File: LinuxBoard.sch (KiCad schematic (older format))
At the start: 0 parts

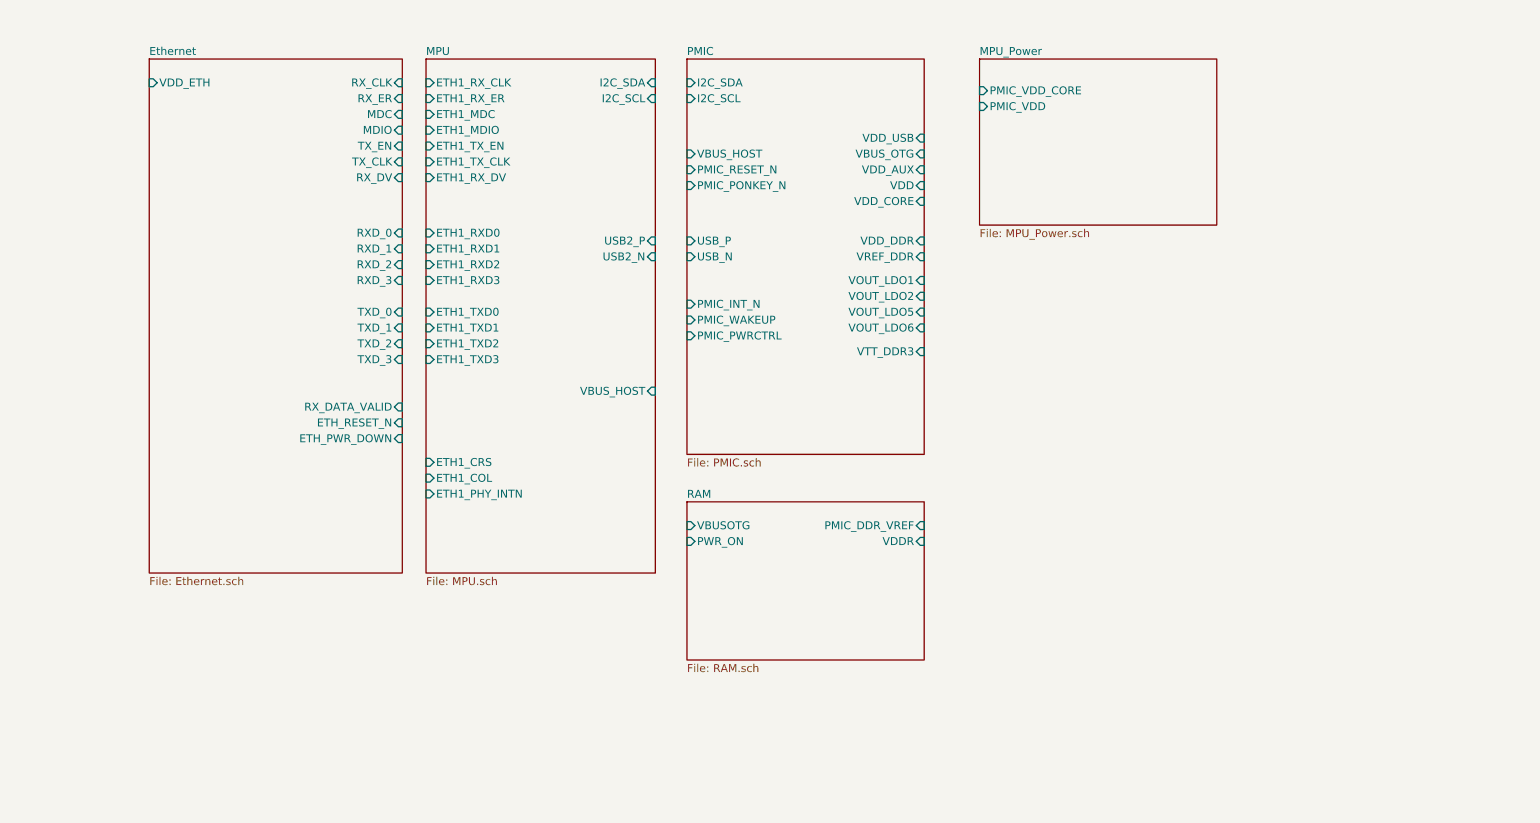
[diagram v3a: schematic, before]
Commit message: Start crossing off ERC. Add generated BOM
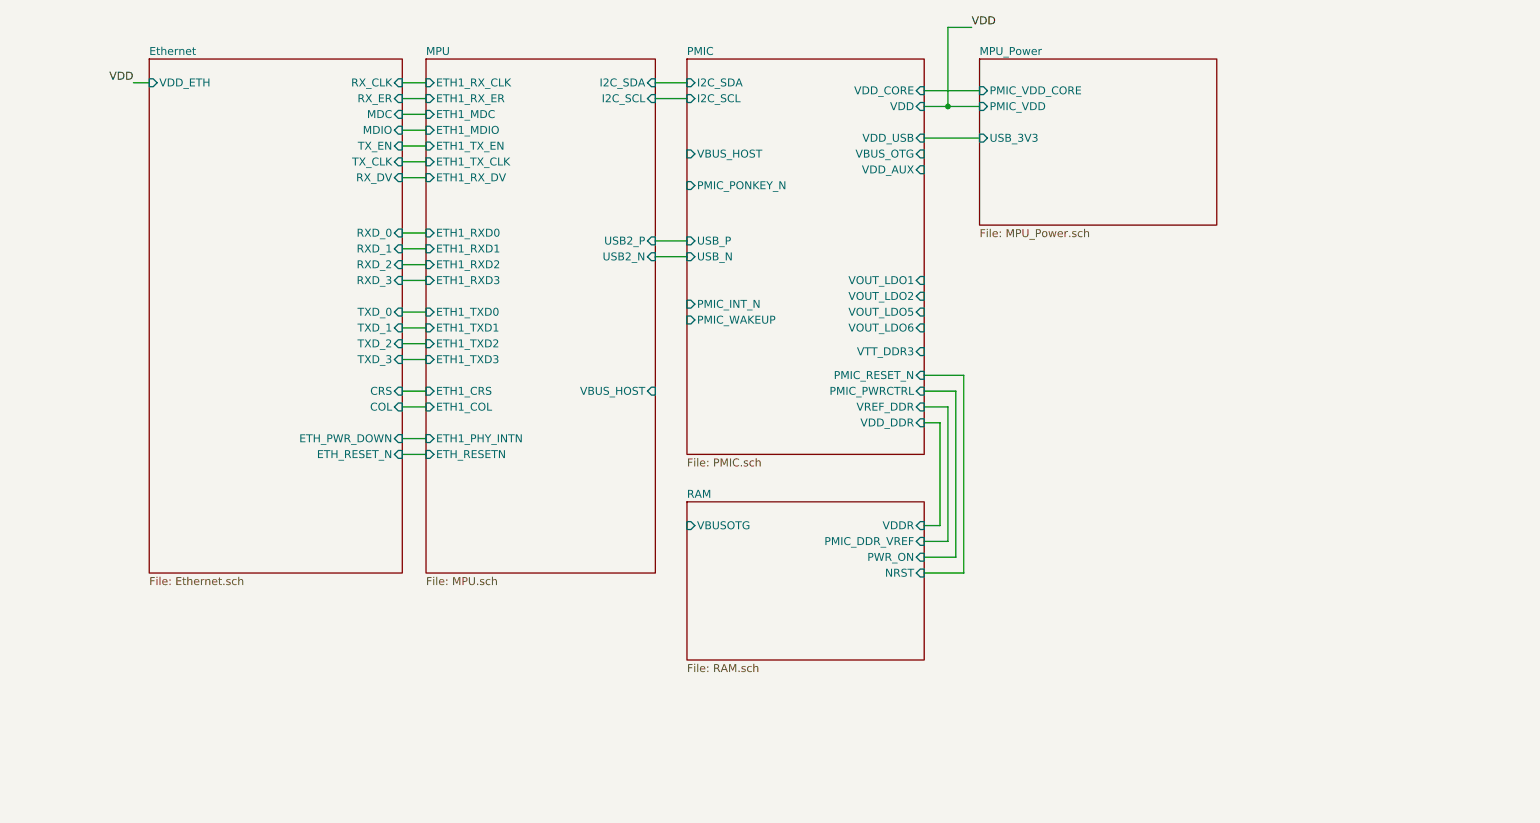
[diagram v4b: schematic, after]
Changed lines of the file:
@@
 F0 "MPU" 50
 F1 "MPU.sch" 50
-F2 "ETH1_CRS" I L 3600 4400 50
+F2 "ETH1_CRS" I L 3600 3950 50
 F3 "ETH1_RX_CLK" I L 3600 2000 50
 F4 "ETH1_MDIO" I L 3600 2300 50
-F5 "ETH1_COL" I L 3600 4500 50
+F5 "ETH1_COL" I L 3600 4050 50
 F6 "ETH1_RX_DV" I L 3600 2600 50
 F7 "ETH1_RXD2" I L 3600 3150 50
@@
 F16 "ETH1_RXD1" I L 3600 3050 50
 F17 "ETH1_TXD3" I L 3600 3750 50
-F18 "ETH1_PHY_INTN" I L 3600 4600 50
+F18 "ETH1_PHY_INTN" I L 3600 4250 50
 F19 "ETH1_TXD0" I L 3600 3450 50
 F20 "I2C_SCL" I R 5050 2100 50
@@
 F23 "USB2_P" I R 5050 3000 50
 F24 "USB2_N" I R 5050 3100 50
+F25 "ETH_RESETN" I L 3600 4350 50
 $EndSheet
 $Sheet
@@
 F2 "PMIC_VDD" I L 7100 2150 50
 F3 "PMIC_VDD_CORE" I L 7100 2050 50
+F4 "USB_3V3" I L 7100 2350 50
 $EndSheet
 $Sheet
@@
 F0 "RAM" 50
 F1 "RAM.sch" 50
-F2 "VDDR" I R 6750 4900 50
-F3 "PMIC_DDR_VREF" I R 6750 4800 50
-F4 "PWR_ON" I L 5250 4900 50
+F2 "VDDR" I R 6750 4800 50
+F3 "PMIC_DDR_VREF" I R 6750 4900 50
+F4 "PWR_ON" I R 6750 5000 50
 F5 "VBUSOTG" I L 5250 4800 50
+F6 "NRST" I R 6750 5100 50
 $EndSheet
 $Sheet
@@
 F4 "VBUS_HOST" I L 5250 2450 50
 F5 "VTT_DDR3" I R 6750 3700 50
-F6 "VREF_DDR" I R 6750 3100 50
+F6 "VREF_DDR" I R 6750 4050 50
 F7 "VOUT_LDO2" I R 6750 3350 50
 F8 "VOUT_LDO1" I R 6750 3250 50
 F9 "VOUT_LDO5" I R 6750 3450 50
 F10 "VOUT_LDO6" I R 6750 3550 50
-F11 "VDD_CORE" I R 6750 2750 50
-F12 "VDD" I R 6750 2650 50
+F11 "VDD_CORE" I R 6750 2050 50
+F12 "VDD" I R 6750 2150 50
 F13 "VDD_AUX" I R 6750 2550 50
-F14 "VDD_DDR" I R 6750 3000 50
+F14 "VDD_DDR" I R 6750 4150 50
 F15 "VDD_USB" I R 6750 2350 50
 F16 "PMIC_PONKEY_N" I L 5250 2650 50
-F17 "PMIC_RESET_N" I L 5250 2550 50
+F17 "PMIC_RESET_N" I R 6750 3850 50
 F18 "PMIC_WAKEUP" I L 5250 3500 50
 F19 "PMIC_INT_N" I L 5250 3400 50
-F20 "PMIC_PWRCTRL" I L 5250 3600 50
+F20 "PMIC_PWRCTRL" I R 6750 3950 50
 F21 "VBUS_OTG" I R 6750 2450 50
 F22 "USB_P" I L 5250 3000 50
@@
 F15 "MDIO" I R 3450 2300 50
 F16 "MDC" I R 3450 2200 50
-F17 "ETH_RESET_N" I R 3450 4150 50
+F17 "ETH_RESET_N" I R 3450 4350 50
 F18 "ETH_PWR_DOWN" I R 3450 4250 50
-F19 "RX_DATA_VALID" I R 3450 4050 50
-F20 "VDD_ETH" I L 1850 2000 50
+F19 "VDD_ETH" I L 1850 2000 50
+F20 "CRS" I R 3450 3950 50
+F21 "COL" I R 3450 4050 50
 $EndSheet
+Wire Wire Line
+	3450 2000 3600 2000
+Wire Wire Line
+	3450 2100 3600 2100
+Wire Wire Line
+	3450 2200 3600 2200
+Wire Wire Line
+	3450 2300 3600 2300
+Wire Wire Line
+	3450 2400 3600 2400
+Wire Wire Line
+	3450 2500 3600 2500
+Wire Wire Line
+	3450 2600 3600 2600
+Wire Wire Line
+	3450 2950 3600 2950
+Wire Wire Line
+	3450 3050 3600 3050
+Wire Wire Line
+	3450 3150 3600 3150
+Wire Wire Line
+	3450 3250 3600 3250
+Wire Wire Line
+	3450 3450 3600 3450
+Wire Wire Line
+	3450 3550 3600 3550
+Wire Wire Line
+	3450 3650 3600 3650
+Wire Wire Line
+	3450 3750 3600 3750
+Wire Wire Line
+	3450 3950 3600 3950
+Wire Wire Line
+	3450 4050 3600 4050
+Wire Wire Line
+	3450 4250 3600 4250
+Wire Wire Line
+	3450 4350 3600 4350
+Wire Wire Line
+	6750 4800 6850 4800
+Wire Wire Line
+	6850 4800 6850 4150
+Wire Wire Line
+	6850 4150 6750 4150
+Wire Wire Line
+	6750 4050 6900 4050
+Wire Wire Line
+	6900 4050 6900 4900
+Wire Wire Line
+	6900 4900 6750 4900
+Wire Wire Line
+	5050 3000 5250 3000
+Wire Wire Line
+	5050 3100 5250 3100
+Wire Wire Line
+	5050 2000 5250 2000
+Wire Wire Line
+	5050 2100 5250 2100
+Wire Wire Line
+	6750 2050 7100 2050
+Wire Wire Line
+	6750 2150 6900 2150
+Wire Wire Line
+	6900 2150 6900 1650
+Wire Wire Line
+	6900 1650 7050 1650
+Connection ~ 6900 2150
+Wire Wire Line
+	6900 2150 7100 2150
+Text Label 7050 1650 0    50   ~ 0
+VDD
+Text Label 1750 2000 2    50   ~ 0
+VDD
+Wire Wire Line
+	1750 2000 1850 2000
+Wire Wire Line
+	6750 2350 7100 2350
+Wire Wire Line
+	6750 5000 6950 5000
+Wire Wire Line
+	6950 5000 6950 3950
+Wire Wire Line
+	6950 3950 6750 3950
+Wire Wire Line
+	6750 5100 7000 5100
+Wire Wire Line
+	7000 5100 7000 3850
+Wire Wire Line
+	7000 3850 6750 3850
 $EndSCHEMATC

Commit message: Complete schematic rough draft
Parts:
- added TP2, TP3, TP? (x11): TestPoint, symbol Connector:TestPoint
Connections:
- net MPU_Power/PMIC_VDD_CORE: now also TP?.1
- net MPU_Power/USB_3V3: now also TP?.1
- net PMIC/VDD_AUX: now also TP?.1
- net PMIC/VOUT_LDO1: now also TP?.1
- net PMIC/VOUT_LDO2: now also TP?.1
- net PMIC/VOUT_LDO5: now also TP?.1
- net PMIC/VOUT_LDO6: now also TP?.1
- net PMIC/VREF_DDR: now also TP?.1
- net VDD: now also TP?.1
- new net GND: TP?.1
- new net MPU_Power/VDDA1V1: TP3.1
- new net MPU_Power/VDDA1V8: TP2.1
- new net MPU_Power/VDDQ_DDR: TP?.1

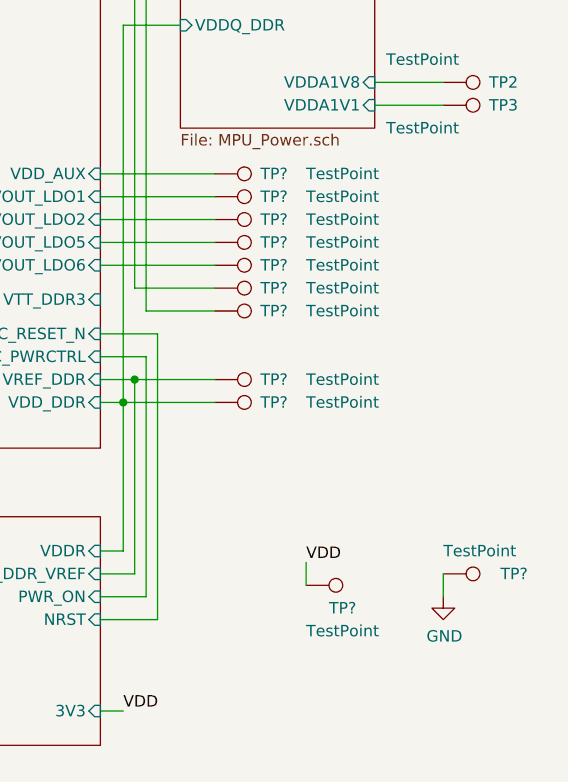
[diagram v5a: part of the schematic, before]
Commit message: Update footprints
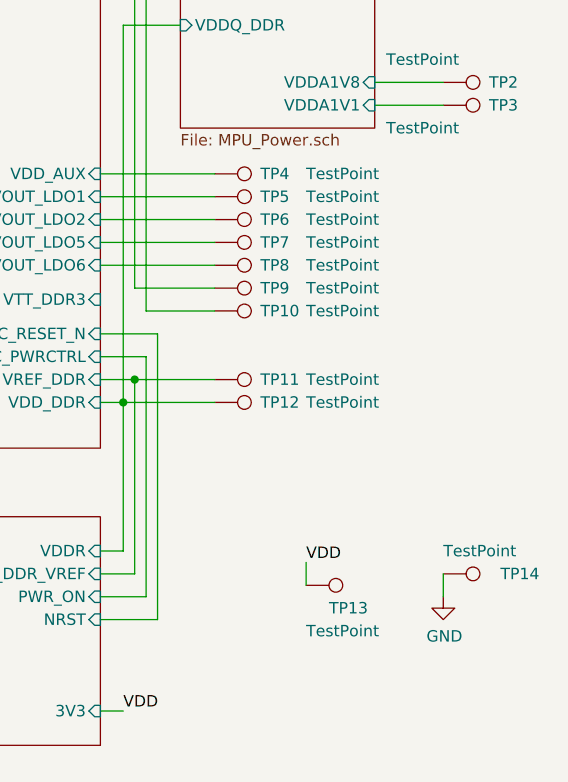
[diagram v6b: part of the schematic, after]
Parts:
- TP10, TP11, TP12, TP13, TP14, TP4, TP5, TP6, TP7, TP8, TP9: renamed from TP?; footprint (none) -> TestPoint:TestPoint_Pad_D2.0mm
- TP2, TP3: footprint (none) -> TestPoint:TestPoint_Pad_D2.0mm
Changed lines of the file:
@@
 F 0 "TP2" V 8250 2950 50  0000 L CNN
 F 1 "TestPoint" V 8150 2500 50  0000 L CNN
-F 2 "" H 8450 2750 50  0001 C CNN
+F 2 "TestPoint:TestPoint_Pad_D2.0mm" H 8450 2750 50  0001 C CNN
 F 3 "~" H 8450 2750 50  0001 C CNN
 	1    8250 2750
@@
 F 0 "TP3" V 8250 3050 50  0000 L CNN
 F 1 "TestPoint" V 8350 2600 50  0000 L CNN
-F 2 "" H 8450 2850 50  0001 C CNN
+F 2 "TestPoint:TestPoint_Pad_D2.0mm" H 8450 2850 50  0001 C CNN
 F 3 "~" H 8450 2850 50  0001 C CNN
 	1    8250 2850
@@
 	8250 2850 7950 2850
 $Comp
-L Connector:TestPoint TP?
+L Connector:TestPoint TP11
 U 1 1 612C0522
 P 7250 4050
-F 0 "TP?" V 7250 4250 50  0000 L CNN
+F 0 "TP11" V 7250 4250 50  0000 L CNN
 F 1 "TestPoint" V 7250 4450 50  0000 L CNN
-F 2 "" H 7450 4050 50  0001 C CNN
+F 2 "TestPoint:TestPoint_Pad_D2.0mm" H 7450 4050 50  0001 C CNN
 F 3 "~" H 7450 4050 50  0001 C CNN
 	1    7250 4050
@@
 	6850 4150 6750 4150
 $Comp
-L Connector:TestPoint TP?
+L Connector:TestPoint TP12
 U 1 1 612BD159
 P 7250 4150
-F 0 "TP?" V 7250 4350 50  0000 L CNN
+F 0 "TP12" V 7250 4350 50  0000 L CNN
 F 1 "TestPoint" V 7250 4550 50  0000 L CNN
-F 2 "" H 7450 4150 50  0001 C CNN
+F 2 "TestPoint:TestPoint_Pad_D2.0mm" H 7450 4150 50  0001 C CNN
 F 3 "~" H 7450 4150 50  0001 C CNN
 	1    7250 4150
@@
 	6850 4150 7250 4150
 $Comp
-L Connector:TestPoint TP?
+L Connector:TestPoint TP7
 U 1 1 612DB861
 P 7250 3450
-F 0 "TP?" V 7250 3650 50  0000 L CNN
+F 0 "TP7" V 7250 3650 50  0000 L CNN
 F 1 "TestPoint" V 7250 3850 50  0000 L CNN
-F 2 "" H 7450 3450 50  0001 C CNN
+F 2 "TestPoint:TestPoint_Pad_D2.0mm" H 7450 3450 50  0001 C CNN
 F 3 "~" H 7450 3450 50  0001 C CNN
 	1    7250 3450
@@
 $EndComp
 $Comp
-L Connector:TestPoint TP?
+L Connector:TestPoint TP8
 U 1 1 612DB867
 P 7250 3550
-F 0 "TP?" V 7250 3750 50  0000 L CNN
+F 0 "TP8" V 7250 3750 50  0000 L CNN
 F 1 "TestPoint" V 7250 3950 50  0000 L CNN
-F 2 "" H 7450 3550 50  0001 C CNN
+F 2 "TestPoint:TestPoint_Pad_D2.0mm" H 7450 3550 50  0001 C CNN
 F 3 "~" H 7450 3550 50  0001 C CNN
 	1    7250 3550
@@
 $EndComp
 $Comp
-L Connector:TestPoint TP?
+L Connector:TestPoint TP5
 U 1 1 612DF154
 P 7250 3250
-F 0 "TP?" V 7250 3450 50  0000 L CNN
+F 0 "TP5" V 7250 3450 50  0000 L CNN
 F 1 "TestPoint" V 7250 3650 50  0000 L CNN
-F 2 "" H 7450 3250 50  0001 C CNN
+F 2 "TestPoint:TestPoint_Pad_D2.0mm" H 7450 3250 50  0001 C CNN
 F 3 "~" H 7450 3250 50  0001 C CNN
 	1    7250 3250
@@
 $EndComp
 $Comp
-L Connector:TestPoint TP?
+L Connector:TestPoint TP6
 U 1 1 612DF15A
 P 7250 3350
-F 0 "TP?" V 7250 3550 50  0000 L CNN
+F 0 "TP6" V 7250 3550 50  0000 L CNN
 F 1 "TestPoint" V 7250 3750 50  0000 L CNN
-F 2 "" H 7450 3350 50  0001 C CNN
+F 2 "TestPoint:TestPoint_Pad_D2.0mm" H 7450 3350 50  0001 C CNN
 F 3 "~" H 7450 3350 50  0001 C CNN
 	1    7250 3350
@@
 	6750 3250 7250 3250
 $Comp
-L Connector:TestPoint TP?
+L Connector:TestPoint TP4
 U 1 1 612E5D6F
 P 7250 3150
-F 0 "TP?" V 7250 3350 50  0000 L CNN
+F 0 "TP4" V 7250 3350 50  0000 L CNN
 F 1 "TestPoint" V 7250 3550 50  0000 L CNN
-F 2 "" H 7450 3150 50  0001 C CNN
+F 2 "TestPoint:TestPoint_Pad_D2.0mm" H 7450 3150 50  0001 C CNN
 F 3 "~" H 7450 3150 50  0001 C CNN
 	1    7250 3150
@@
 VDD
 $Comp
-L Connector:TestPoint TP?
+L Connector:TestPoint TP13
 U 1 1 612EBF28
 P 7650 4950
-F 0 "TP?" V 7750 5050 50  0000 L CNN
+F 0 "TP13" V 7750 5050 50  0000 L CNN
 F 1 "TestPoint" V 7850 4950 50  0000 L CNN
-F 2 "" H 7850 4950 50  0001 C CNN
+F 2 "TestPoint:TestPoint_Pad_D2.0mm" H 7850 4950 50  0001 C CNN
 F 3 "~" H 7850 4950 50  0001 C CNN
 	1    7650 4950
@@
 	7650 4950 7650 4850
 $Comp
-L power:GND #PWR?
+L power:GND #PWR040
 U 1 1 612F3316
 P 8250 5000
-F 0 "#PWR?" H 8250 4750 50  0001 C CNN
+F 0 "#PWR040" H 8250 4750 50  0001 C CNN
 F 1 "GND" H 8255 4827 50  0000 C CNN
 F 2 "" H 8250 5000 50  0001 C CNN
@@
 $EndComp
 $Comp
-L Connector:TestPoint TP?
+L Connector:TestPoint TP14
 U 1 1 612F451D
 P 8250 4900
-F 0 "TP?" V 8250 5150 50  0000 L CNN
+F 0 "TP14" V 8250 5150 50  0000 L CNN
 F 1 "TestPoint" V 8150 4900 50  0000 L CNN
-F 2 "" H 8450 4900 50  0001 C CNN
+F 2 "TestPoint:TestPoint_Pad_D2.0mm" H 8450 4900 50  0001 C CNN
 F 3 "~" H 8450 4900 50  0001 C CNN
 	1    8250 4900
@@
 	8250 4900 8250 5000
 $Comp
-L Connector:TestPoint TP?
+L Connector:TestPoint TP9
 U 1 1 612F9AD0
 P 7250 3650
-F 0 "TP?" V 7250 3850 50  0000 L CNN
+F 0 "TP9" V 7250 3850 50  0000 L CNN
 F 1 "TestPoint" V 7250 4050 50  0000 L CNN
-F 2 "" H 7450 3650 50  0001 C CNN
+F 2 "TestPoint:TestPoint_Pad_D2.0mm" H 7450 3650 50  0001 C CNN
 F 3 "~" H 7450 3650 50  0001 C CNN
 	1    7250 3650
@@
 	6900 2350 7100 2350
 $Comp
-L Connector:TestPoint TP?
+L Connector:TestPoint TP10
 U 1 1 612FFBBE
 P 7250 3750
-F 0 "TP?" V 7250 3950 50  0000 L CNN
+F 0 "TP10" V 7250 3950 50  0000 L CNN
 F 1 "TestPoint" V 7250 4150 50  0000 L CNN
-F 2 "" H 7450 3750 50  0001 C CNN
+F 2 "TestPoint:TestPoint_Pad_D2.0mm" H 7450 3750 50  0001 C CNN
 F 3 "~" H 7450 3750 50  0001 C CNN
 	1    7250 3750

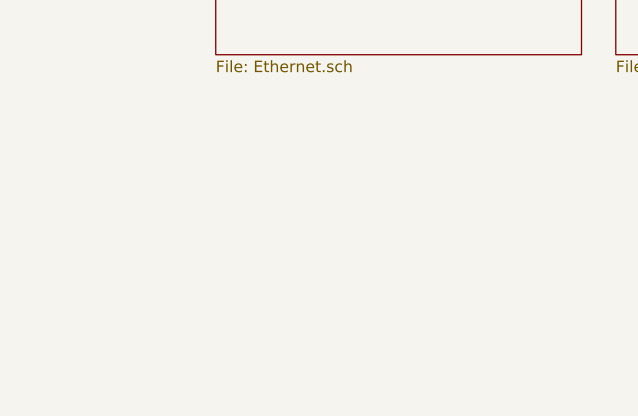
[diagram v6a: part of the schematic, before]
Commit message: Add mounting holes
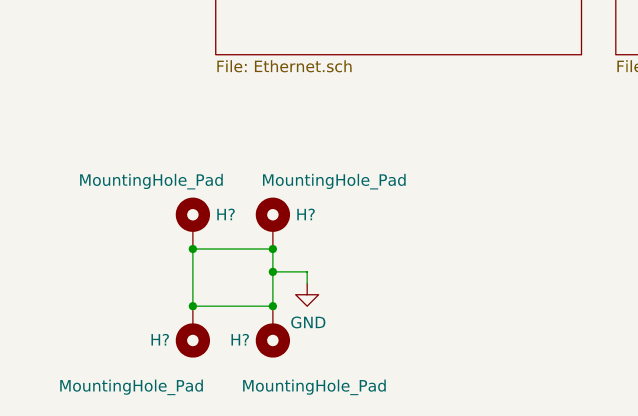
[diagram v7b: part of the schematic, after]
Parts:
- added H? (x4): MountingHole_Pad, symbol Mechanical:MountingHole_Pad
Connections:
- net GND: now also H?.1, H?.1, H?.1, H?.1
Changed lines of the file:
@@
 Wire Wire Line
 	6950 2050 7100 2050
+$Comp
+L Mechanical:MountingHole_Pad H?
+U 1 1 60E8FE8D
+P 2100 5850
+F 0 "H?" H 2200 5899 50  0000 L CNN
+F 1 "MountingHole_Pad" H 2050 6050 50  0000 L CNN
+F 2 "" H 2100 5850 50  0001 C CNN
+F 3 "~" H 2100 5850 50  0001 C CNN
+	1    2100 5850
+	1    0    0    -1
+$EndComp
+$Comp
+L Mechanical:MountingHole_Pad H?
+U 1 1 60E9127A
+P 1750 6300
+F 0 "H?" H 1850 6349 50  0000 L CNN
+F 1 "MountingHole_Pad" H 1700 6550 50  0000 L CNN
+F 2 "" H 1750 6300 50  0001 C CNN
+F 3 "~" H 1750 6300 50  0001 C CNN
+	1    1750 6300
+	-1   0    0    1
+$EndComp
+$Comp
+L Mechanical:MountingHole_Pad H?
+U 1 1 60E9329A
+P 2100 6300
+F 0 "H?" H 2200 6349 50  0000 L CNN
+F 1 "MountingHole_Pad" H 1600 6550 50  0000 L CNN
+F 2 "" H 2100 6300 50  0001 C CNN
+F 3 "~" H 2100 6300 50  0001 C CNN
+	1    2100 6300
+	-1   0    0    1
+$EndComp
+$Comp
+L Mechanical:MountingHole_Pad H?
+U 1 1 60E95D0C
+P 1750 5850
+F 0 "H?" H 1850 5899 50  0000 L CNN
+F 1 "MountingHole_Pad" H 1250 6050 50  0000 L CNN
+F 2 "" H 1750 5850 50  0001 C CNN
+F 3 "~" H 1750 5850 50  0001 C CNN
+	1    1750 5850
+	1    0    0    -1
+$EndComp
+Wire Wire Line
+	2100 5950 1750 5950
+Wire Wire Line
+	1750 5950 1750 6200
+Connection ~ 1750 5950
+Wire Wire Line
+	1750 6200 2100 6200
+Wire Wire Line
+	2100 6200 2100 6050
+Connection ~ 1750 6200
+Connection ~ 2100 6200
+Connection ~ 2100 5950
+Wire Wire Line
+	2100 6050 2250 6050
+Wire Wire Line
+	2250 6050 2250 6100
+Connection ~ 2100 6050
+Wire Wire Line
+	2100 6050 2100 5950
+$Comp
+L power:GND #PWR?
+U 1 1 60E9D149
+P 2250 6100
+F 0 "#PWR?" H 2250 5850 50  0001 C CNN
+F 1 "GND" H 2255 5927 50  0000 C CNN
+F 2 "" H 2250 6100 50  0001 C CNN
+F 3 "" H 2250 6100 50  0001 C CNN
+	1    2250 6100
+	1    0    0    -1
+$EndComp
 $EndSCHEMATC
